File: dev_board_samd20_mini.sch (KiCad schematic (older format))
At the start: 9 parts, among them J1 Conn_02x05_Odd_Even, J2 Conn_02x08, J3 Conn_01x10, J4 Conn_02x08, U1 SAMD20G18A-AU

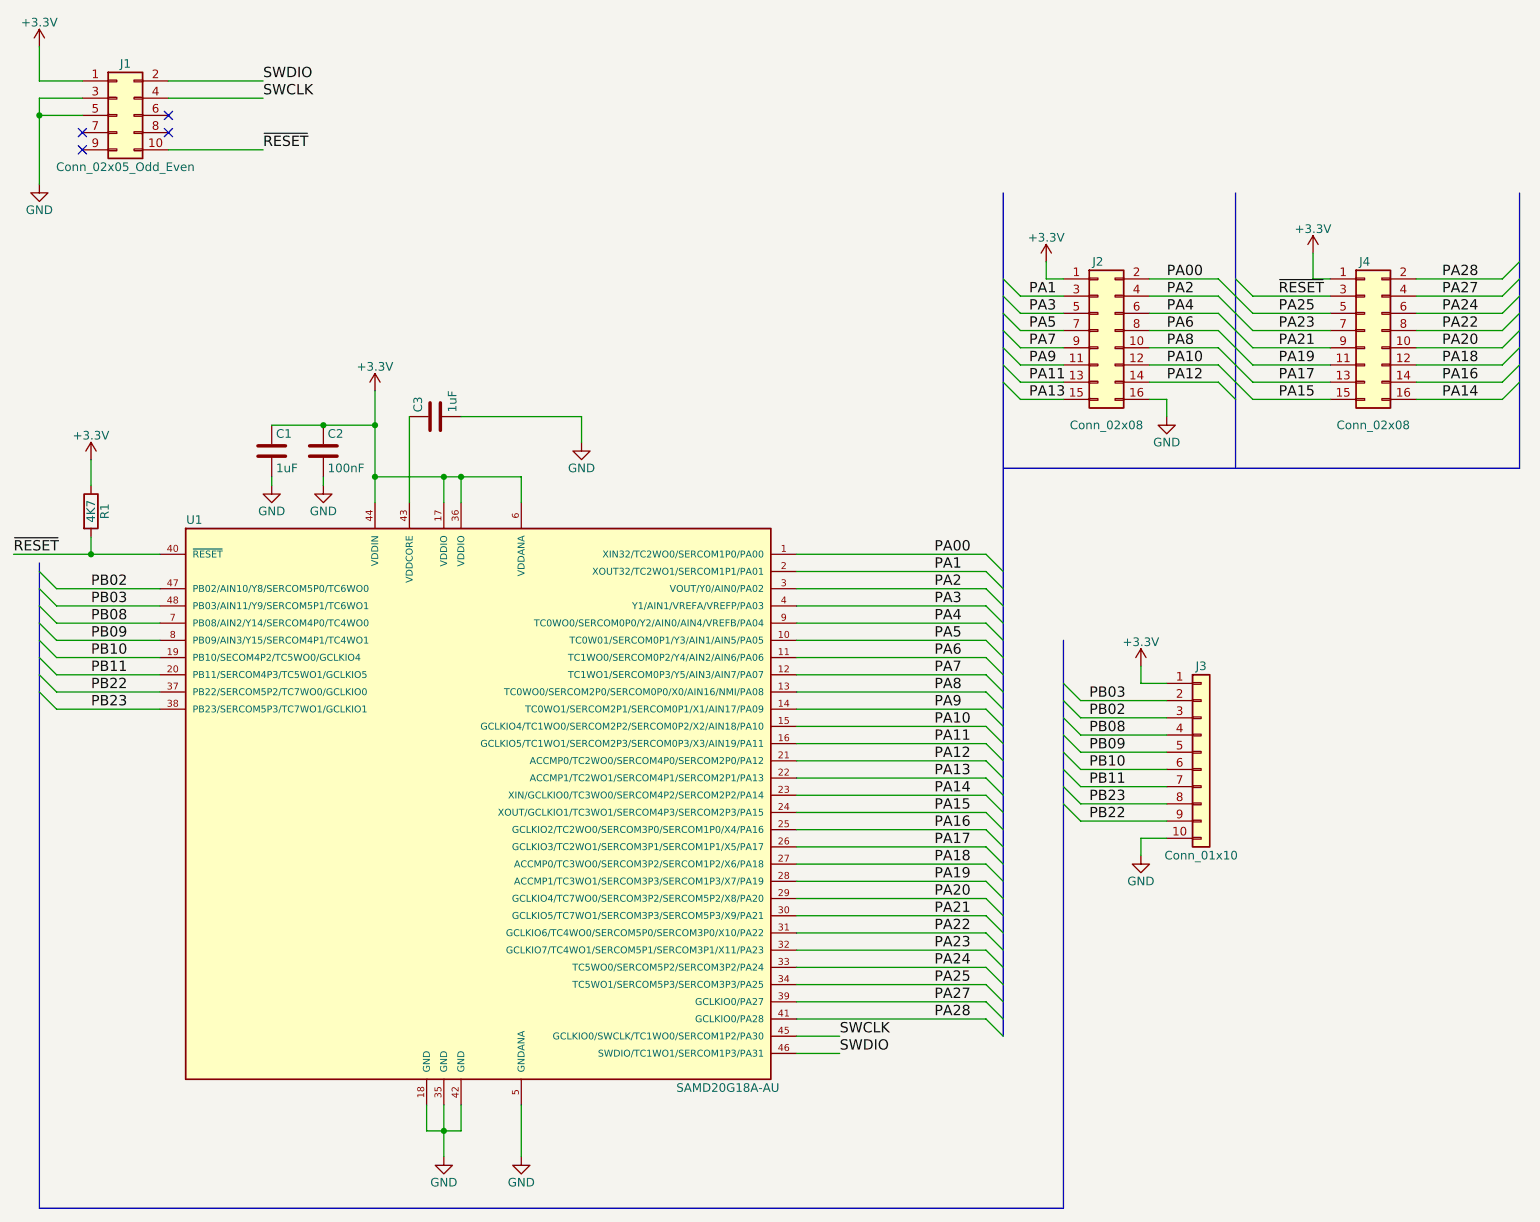
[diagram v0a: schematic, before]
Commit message: Réduction de la taille de la carte
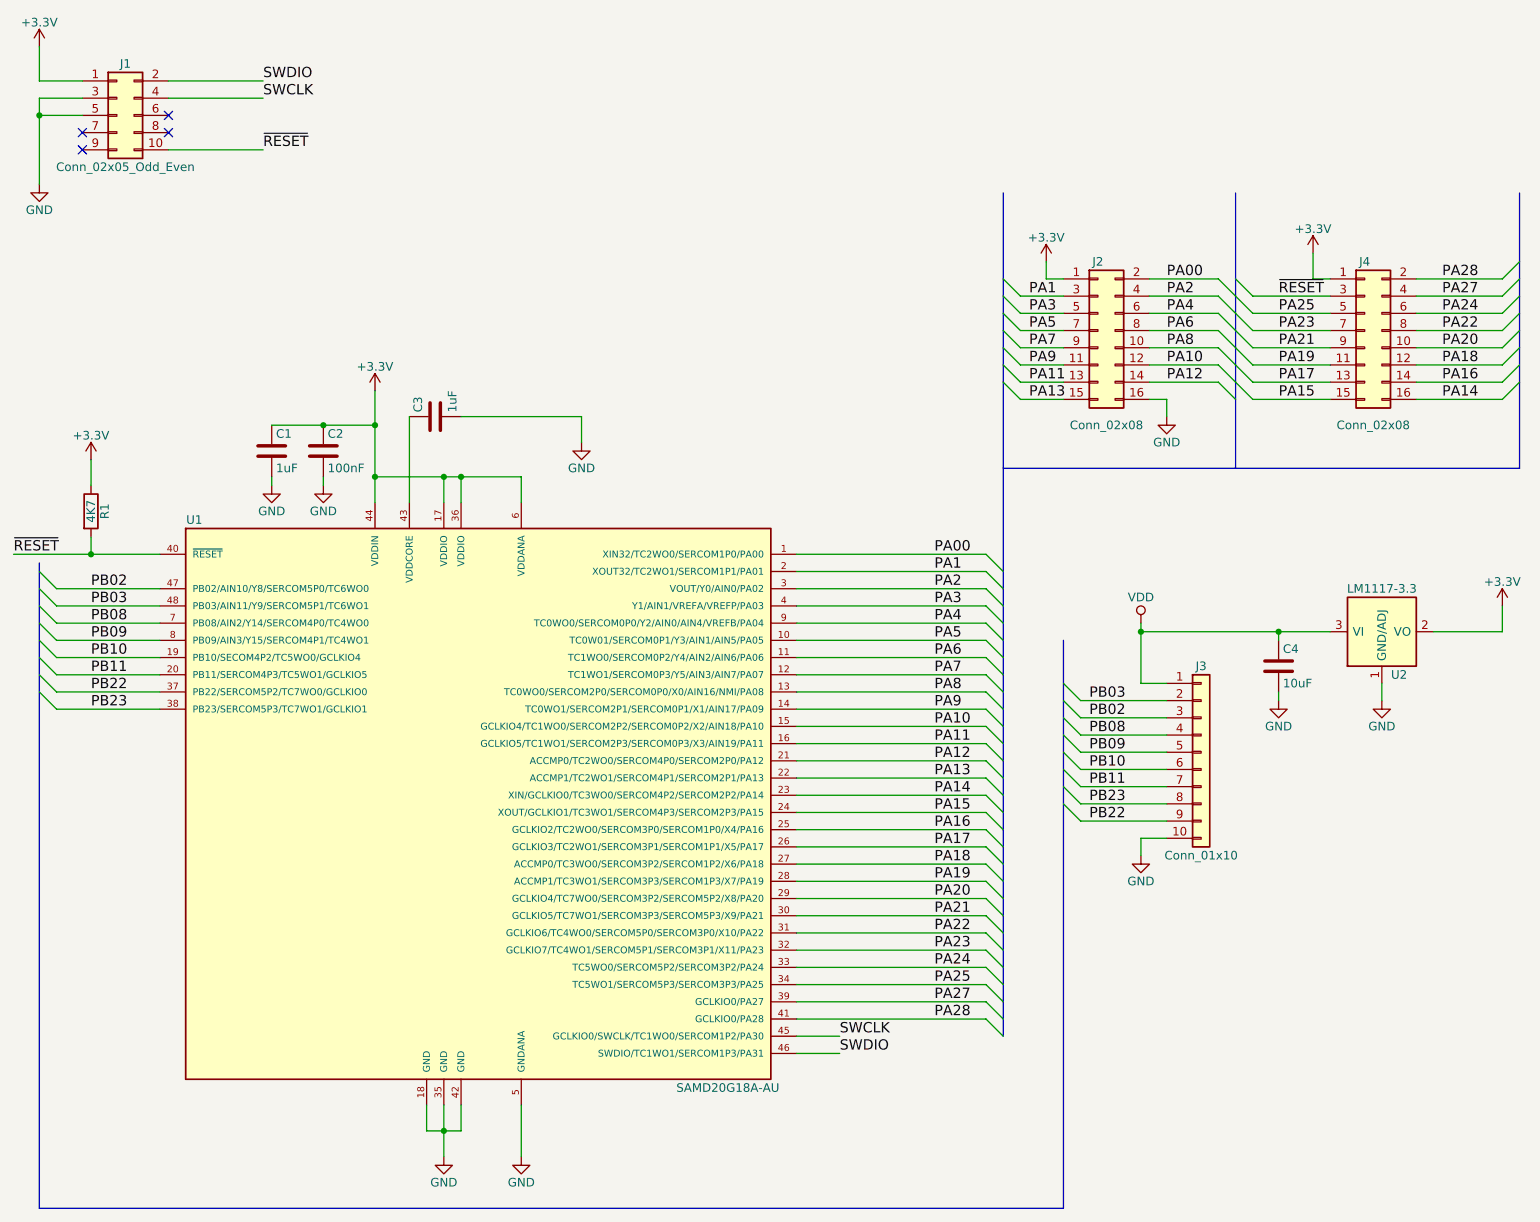
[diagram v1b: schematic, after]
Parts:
- added C4: 10uF, Capacitors_SMD:C_0805, symbol C
- added U2: LM1117-3.3, TO_SOT_Packages_SMD:SOT-223, symbol LM1117-3.3
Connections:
- net +3V3: now also U2.2 (VO), U2.4 (VO); no longer J3.1 (Pin_1)
- net GND: now also C4.2, U2.1 (GND/ADJ)
- new net VDD: C4.1, J3.1 (Pin_1), U2.3 (VI)
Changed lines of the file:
@@
 	6800 4250 6800 7550
 Wire Bus Line
-	850  7550 6800 7550
-Wire Bus Line
-	850  3800 850  7550
+	6800 7550 850  7550
+Wire Bus Line
+	850  7550 850  3800
 Wire Wire Line
 	1550 4650 950  4650
@@
 	6900 5300 7400 5300
 $Comp
-L +3.3V #PWR013
-U 1 1 5AA4E83B
-P 7250 4400
-F 0 "#PWR013" H 7250 4250 50  0001 C CNN
-F 1 "+3.3V" H 7250 4540 50  0000 C CNN
-F 2 "" H 7250 4400 50  0001 C CNN
-F 3 "" H 7250 4400 50  0001 C CNN
-	1    7250 4400
-	1    0    0    -1
-$EndComp
-$Comp
-L GND #PWR014
+L GND #PWR013
 U 1 1 5AA4E873
 P 7250 5500
-F 0 "#PWR014" H 7250 5250 50  0001 C CNN
+F 0 "#PWR013" H 7250 5250 50  0001 C CNN
 F 1 "GND" H 7250 5350 50  0000 C CNN
 F 2 "" H 7250 5500 50  0001 C CNN
@@
 	7400 4500 7250 4500
 Wire Wire Line
-	7250 4500 7250 4400
+	7250 4500 7250 4150
 Text Label 6950 4600 0    60   ~ 0
 PB03
@@
 Text Label 9000 2850 0    60   ~ 0
 PA14
+$Comp
+L LM1117-3.3 U2
+U 1 1 5AA63981
+P 8650 4200
+F 0 "U2" H 8750 3950 50  0000 C CNN
+F 1 "LM1117-3.3" H 8650 4450 50  0000 C CNN
+F 2 "TO_SOT_Packages_SMD:SOT-223" H 8650 4200 50  0001 C CNN
+F 3 "" H 8650 4200 50  0000 C CNN
+	1    8650 4200
+	1    0    0    -1
+$EndComp
+$Comp
+L VDD #PWR014
+U 1 1 5AA63B60
+P 7250 4150
+F 0 "#PWR014" H 7250 4000 50  0001 C CNN
+F 1 "VDD" H 7250 4300 50  0000 C CNN
+F 2 "" H 7250 4150 50  0000 C CNN
+F 3 "" H 7250 4150 50  0000 C CNN
+	1    7250 4150
+	1    0    0    -1
+$EndComp
+Wire Wire Line
+	7250 4200 8350 4200
+Connection ~ 7250 4200
+$Comp
+L C C4
+U 1 1 5AA63F1F
+P 8050 4400
+F 0 "C4" H 8075 4500 50  0000 L CNN
+F 1 "10uF" H 8075 4300 50  0000 L CNN
+F 2 "Capacitors_SMD:C_0805" H 8088 4250 50  0001 C CNN
+F 3 "" H 8050 4400 50  0001 C CNN
+	1    8050 4400
+	1    0    0    -1
+$EndComp
+Wire Wire Line
+	8050 4250 8050 4200
+Connection ~ 8050 4200
+$Comp
+L GND #PWR015
+U 1 1 5AA64114
+P 8050 4600
+F 0 "#PWR015" H 8050 4350 50  0001 C CNN
+F 1 "GND" H 8050 4450 50  0000 C CNN
+F 2 "" H 8050 4600 50  0001 C CNN
+F 3 "" H 8050 4600 50  0001 C CNN
+	1    8050 4600
+	1    0    0    -1
+$EndComp
+Wire Wire Line
+	8050 4600 8050 4550
+$Comp
+L GND #PWR016
+U 1 1 5AA641D0
+P 8650 4600
+F 0 "#PWR016" H 8650 4350 50  0001 C CNN
+F 1 "GND" H 8650 4450 50  0000 C CNN
+F 2 "" H 8650 4600 50  0001 C CNN
+F 3 "" H 8650 4600 50  0001 C CNN
+	1    8650 4600
+	1    0    0    -1
+$EndComp
+Wire Wire Line
+	8650 4600 8650 4500
+Wire Wire Line
+	8950 4200 9350 4200
+$Comp
+L +3.3V #PWR017
+U 1 1 5AA64383
+P 9350 4050
+F 0 "#PWR017" H 9350 3900 50  0001 C CNN
+F 1 "+3.3V" H 9350 4190 50  0000 C CNN
+F 2 "" H 9350 4050 50  0001 C CNN
+F 3 "" H 9350 4050 50  0001 C CNN
+	1    9350 4050
+	1    0    0    -1
+$EndComp
+Wire Wire Line
+	9350 4200 9350 4050
 $EndSCHEMATC
